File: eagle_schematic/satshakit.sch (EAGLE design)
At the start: 16 parts

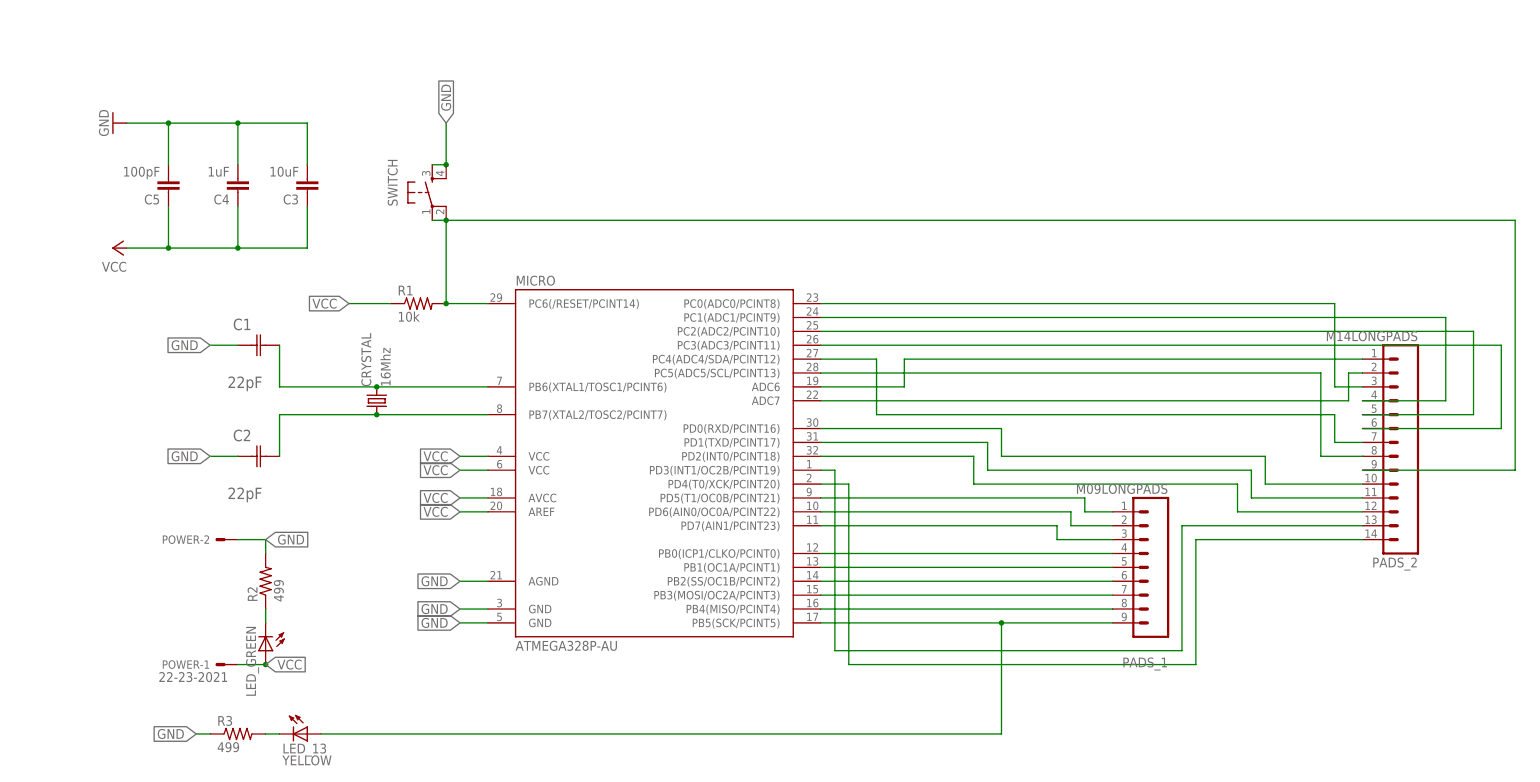
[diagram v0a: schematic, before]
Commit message: v0.2 programming from FTDI cable
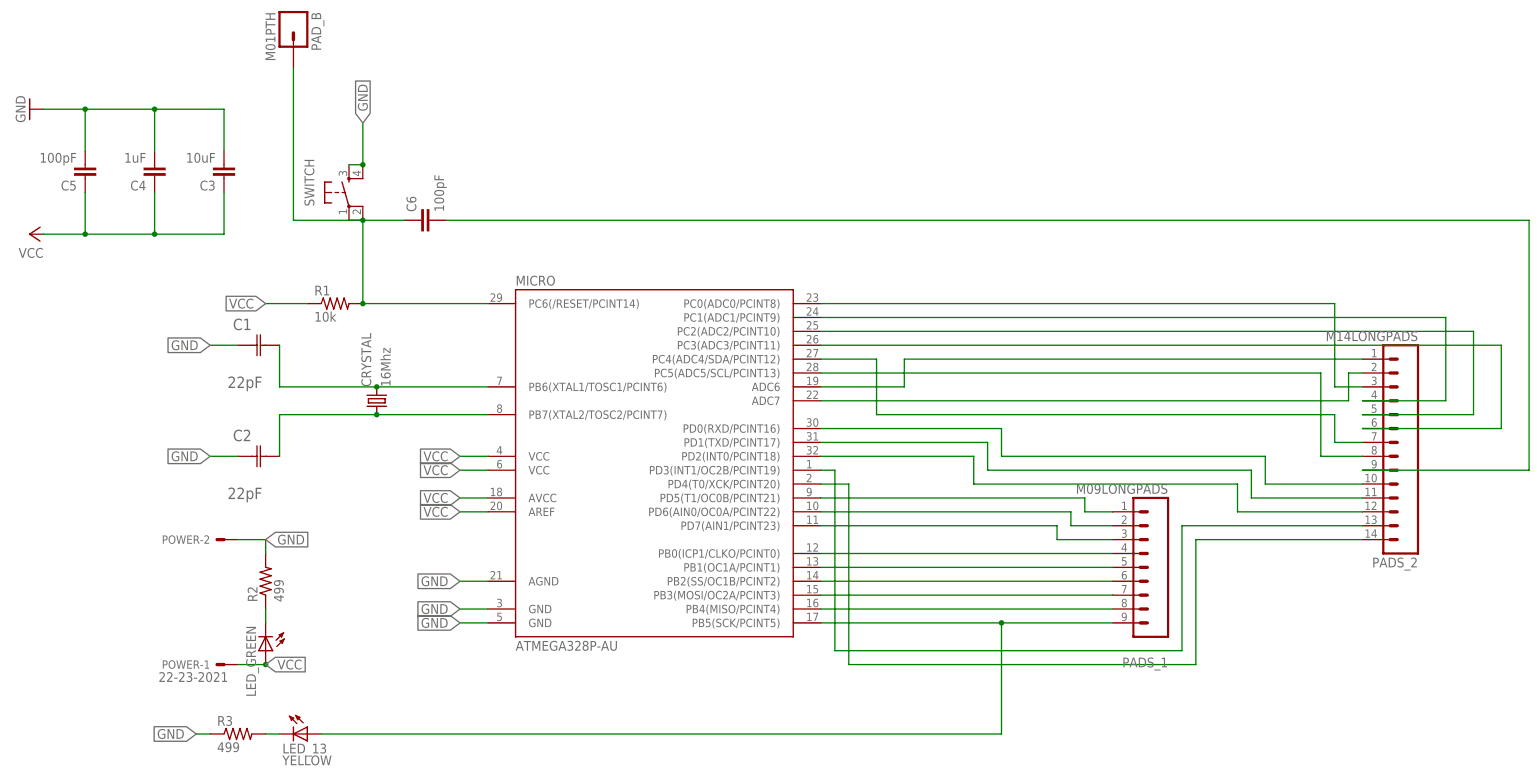
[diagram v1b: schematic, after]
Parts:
- added C6: 100pF, 01_SparkFun:CAP1206
- added PAD_B: M01PTH, 01_SparkFun:M01PTH
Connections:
- new net N$28: C6.1, MICRO.PC6(/RESET/PCINT14), PAD_B.1, R1.2, SWITCH.P, SWITCH.P1
- net N$3: now also C6.2; no longer MICRO.PC6(/RESET/PCINT14), R1.2, SWITCH.P, SWITCH.P1
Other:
- moved on the sheet: C3, C4, C5, R1, SWITCH
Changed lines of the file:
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@@
 <part name="C4" library="01_SparkFun" deviceset="CAP" device="1206" value="1uF"/>
 <part name="C5" library="01_SparkFun" deviceset="CAP" device="1206" value="100pF"/>
+<part name="C6" library="01_SparkFun" deviceset="CAP" device="1206" value="100pF"/>
+<part name="PAD_B" library="01_SparkFun" deviceset="M01" device="PTH"/>
 </parts>
 <sheets>
@@
 <instances>
 <instance part="MICRO" gate="1" x="40.64" y="50.8"/>
-<instance part="P+7" gate="VCC" x="-58.42" y="88.9" rot="R90"/>
+<instance part="P+7" gate="VCC" x="-73.66" y="91.44" rot="R90"/>
 <instance part="CRYSTAL" gate="P" x="-10.16" y="60.96" rot="R90"/>
 <instance part="C1" gate="A" x="-35.56" y="71.12"/>
 <instance part="C2" gate="A" x="-35.56" y="50.8"/>
-<instance part="GND1" gate="1" x="-58.42" y="111.76" rot="R270"/>
-<instance part="R1" gate="G$1" x="-2.54" y="78.74"/>
-<instance part="SWITCH" gate="2" x="0" y="99.06"/>
+<instance part="GND1" gate="1" x="-73.66" y="114.3" rot="R270"/>
+<instance part="R1" gate="G$1" x="-17.78" y="78.74"/>
+<instance part="SWITCH" gate="2" x="-15.24" y="99.06"/>
 <instance part="POWER" gate="-1" x="-38.1" y="12.7" rot="R180"/>
 <instance part="POWER" gate="-2" x="-38.1" y="35.56" rot="R180"/>
@@
 <instance part="R2" gate="G$1" x="-30.48" y="27.94" rot="R90"/>
 <instance part="R3" gate="G$1" x="-35.56" y="0"/>
-<instance part="C3" gate="G$1" x="-22.86" y="101.6" rot="R180"/>
-<instance part="C4" gate="G$1" x="-35.56" y="101.6" rot="R180"/>
-<instance part="C5" gate="G$1" x="-48.26" y="101.6" rot="R180"/>
+<instance part="C3" gate="G$1" x="-38.1" y="104.14" rot="R180"/>
+<instance part="C4" gate="G$1" x="-50.8" y="104.14" rot="R180"/>
+<instance part="C5" gate="G$1" x="-63.5" y="104.14" rot="R180"/>
+<instance part="C6" gate="G$1" x="0" y="93.98" rot="R90"/>
+<instance part="PAD_B" gate="G$1" x="-25.4" y="129.54" rot="R270"/>
 </instances>
 <busses>
@@
 <segment>
 <pinref part="R1" gate="G$1" pin="1"/>
-<wire x1="-7.62" y1="78.74" x2="-15.24" y2="78.74" width="0.1524" layer="91"/>
-<label x="-15.24" y="78.74" size="1.778" layer="95" rot="R180" xref="yes"/>
+<wire x1="-22.86" y1="78.74" x2="-30.48" y2="78.74" width="0.1524" layer="91"/>
+<label x="-30.48" y="78.74" size="1.778" layer="95" rot="R180" xref="yes"/>
 </segment>
 <segment>
@@
 <segment>
 <pinref part="P+7" gate="VCC" pin="VCC"/>
-<wire x1="-55.88" y1="88.9" x2="-48.26" y2="88.9" width="0.1524" layer="91"/>
-<wire x1="-48.26" y1="88.9" x2="-35.56" y2="88.9" width="0.1524" layer="91"/>
+<wire x1="-71.12" y1="91.44" x2="-63.5" y2="91.44" width="0.1524" layer="91"/>
+<wire x1="-63.5" y1="91.44" x2="-50.8" y2="91.44" width="0.1524" layer="91"/>
 <pinref part="C4" gate="G$1" pin="1"/>
-<wire x1="-22.86" y1="88.9" x2="-35.56" y2="88.9" width="0.1524" layer="91"/>
-<wire x1="-35.56" y1="96.52" x2="-35.56" y2="88.9" width="0.1524" layer="91"/>
-<junction x="-35.56" y="88.9"/>
+<wire x1="-38.1" y1="91.44" x2="-50.8" y2="91.44" width="0.1524" layer="91"/>
+<wire x1="-50.8" y1="99.06" x2="-50.8" y2="91.44" width="0.1524" layer="91"/>
+<junction x="-50.8" y="91.44"/>
 <pinref part="C5" gate="G$1" pin="1"/>
-<wire x1="-48.26" y1="96.52" x2="-48.26" y2="88.9" width="0.1524" layer="91"/>
-<junction x="-48.26" y="88.9"/>
+<wire x1="-63.5" y1="99.06" x2="-63.5" y2="91.44" width="0.1524" layer="91"/>
+<junction x="-63.5" y="91.44"/>
 <pinref part="C3" gate="G$1" pin="1"/>
-<wire x1="-22.86" y1="96.52" x2="-22.86" y2="88.9" width="0.1524" layer="91"/>
+<wire x1="-38.1" y1="99.06" x2="-38.1" y2="91.44" width="0.1524" layer="91"/>
 </segment>
 </net>
@@
 <segment>
 <pinref part="GND1" gate="1" pin="GND"/>
-<wire x1="-55.88" y1="111.76" x2="-48.26" y2="111.76" width="0.1524" layer="91"/>
-<wire x1="-48.26" y1="111.76" x2="-35.56" y2="111.76" width="0.1524" layer="91"/>
-<wire x1="-35.56" y1="111.76" x2="-22.86" y2="111.76" width="0.1524" layer="91"/>
-<wire x1="-48.26" y1="104.14" x2="-48.26" y2="111.76" width="0.1524" layer="91"/>
-<junction x="-48.26" y="111.76"/>
-<wire x1="-35.56" y1="104.14" x2="-35.56" y2="111.76" width="0.1524" layer="91"/>
-<junction x="-35.56" y="111.76"/>
+<wire x1="-71.12" y1="114.3" x2="-63.5" y2="114.3" width="0.1524" layer="91"/>
+<wire x1="-63.5" y1="114.3" x2="-50.8" y2="114.3" width="0.1524" layer="91"/>
+<wire x1="-50.8" y1="114.3" x2="-38.1" y2="114.3" width="0.1524" layer="91"/>
+<wire x1="-63.5" y1="106.68" x2="-63.5" y2="114.3" width="0.1524" layer="91"/>
+<junction x="-63.5" y="114.3"/>
+<wire x1="-50.8" y1="106.68" x2="-50.8" y2="114.3" width="0.1524" layer="91"/>
+<junction x="-50.8" y="114.3"/>
 <pinref part="C4" gate="G$1" pin="2"/>
 <pinref part="C5" gate="G$1" pin="2"/>
 <pinref part="C3" gate="G$1" pin="2"/>
-<wire x1="-22.86" y1="104.14" x2="-22.86" y2="111.76" width="0.1524" layer="91"/>
+<wire x1="-38.1" y1="106.68" x2="-38.1" y2="114.3" width="0.1524" layer="91"/>
 </segment>
 <segment>
@@
 <pinref part="SWITCH" gate="2" pin="S"/>
 <pinref part="SWITCH" gate="2" pin="S1"/>
-<wire x1="0" y1="104.14" x2="2.54" y2="104.14" width="0.1524" layer="91"/>
-<wire x1="2.54" y1="104.14" x2="2.54" y2="111.76" width="0.1524" layer="91"/>
-<junction x="2.54" y="104.14"/>
-<label x="2.54" y="111.76" size="1.778" layer="95" rot="R90" xref="yes"/>
+<wire x1="-15.24" y1="104.14" x2="-12.7" y2="104.14" width="0.1524" layer="91"/>
+<wire x1="-12.7" y1="104.14" x2="-12.7" y2="111.76" width="0.1524" layer="91"/>
+<junction x="-12.7" y="104.14"/>
+<label x="-12.7" y="111.76" size="1.778" layer="95" rot="R90" xref="yes"/>
 </segment>
 <segment>
@@
 <wire x1="-40.64" y1="0" x2="-43.18" y2="0" width="0.1524" layer="91"/>
 <label x="-43.18" y="0" size="1.778" layer="95" rot="R180" xref="yes"/>
-</segment>
-</net>
-<net name="N$3" class="0">
-<segment>
-<pinref part="MICRO" gate="1" pin="PC6(/RESET/PCINT14)"/>
-<wire x1="10.16" y1="78.74" x2="2.54" y2="78.74" width="0.1524" layer="91"/>
-<pinref part="R1" gate="G$1" pin="2"/>
-<wire x1="2.54" y1="78.74" x2="2.54" y2="93.98" width="0.1524" layer="91"/>
-<junction x="2.54" y="78.74"/>
-<pinref part="SWITCH" gate="2" pin="P1"/>
-<pinref part="SWITCH" gate="2" pin="P"/>
-<wire x1="2.54" y1="93.98" x2="0" y2="93.98" width="0.1524" layer="91"/>
-<junction x="2.54" y="93.98"/>
-<wire x1="2.54" y1="93.98" x2="198.12" y2="93.98" width="0.1524" layer="91"/>
-<wire x1="198.12" y1="93.98" x2="198.12" y2="48.26" width="0.1524" layer="91"/>
-<pinref part="PADS_2" gate="G$1" pin="9"/>
-<wire x1="198.12" y1="48.26" x2="170.18" y2="48.26" width="0.1524" layer="91"/>
 </segment>
 </net>
@@
 </segment>
 </net>
+<net name="N$28" class="0">
+<segment>
+<pinref part="SWITCH" gate="2" pin="P"/>
+<pinref part="SWITCH" gate="2" pin="P1"/>
+<wire x1="-12.7" y1="93.98" x2="-15.24" y2="93.98" width="0.1524" layer="91"/>
+<junction x="-12.7" y="93.98"/>
+<pinref part="R1" gate="G$1" pin="2"/>
+<wire x1="-12.7" y1="78.74" x2="-12.7" y2="93.98" width="0.1524" layer="91"/>
+<wire x1="-12.7" y1="93.98" x2="-5.08" y2="93.98" width="0.1524" layer="91"/>
+<junction x="-12.7" y="78.74"/>
+<pinref part="MICRO" gate="1" pin="PC6(/RESET/PCINT14)"/>
+<wire x1="10.16" y1="78.74" x2="-12.7" y2="78.74" width="0.1524" layer="91"/>
+<pinref part="C6" gate="G$1" pin="1"/>
+<wire x1="-12.7" y1="93.98" x2="-25.4" y2="93.98" width="0.1524" layer="91"/>
+<wire x1="-25.4" y1="93.98" x2="-25.4" y2="121.92" width="0.1524" layer="91"/>
+<pinref part="PAD_B" gate="G$1" pin="1"/>
+</segment>
+</net>
+<net name="N$3" class="0">
+<segment>
+<pinref part="PADS_2" gate="G$1" pin="9"/>
+<wire x1="200.66" y1="93.98" x2="200.66" y2="48.26" width="0.1524" layer="91"/>
+<wire x1="200.66" y1="48.26" x2="170.18" y2="48.26" width="0.1524" layer="91"/>
+<pinref part="C6" gate="G$1" pin="2"/>
+<wire x1="2.54" y1="93.98" x2="200.66" y2="93.98" width="0.1524" layer="91"/>
+</segment>
+</net>

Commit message: minor fixes
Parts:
- C6: value 100pF -> 100nF
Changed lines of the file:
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@@
 <part name="C4" library="01_SparkFun" deviceset="CAP" device="1206" value="1uF"/>
 <part name="C5" library="01_SparkFun" deviceset="CAP" device="1206" value="100pF"/>
-<part name="C6" library="01_SparkFun" deviceset="CAP" device="1206" value="100pF"/>
+<part name="C6" library="01_SparkFun" deviceset="CAP" device="1206" value="100nF"/>
 <part name="PAD_B" library="01_SparkFun" deviceset="M01" device="PTH"/>
 </parts>

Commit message: minor fixes
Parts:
- C5: value 100pF -> 100nF
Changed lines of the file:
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@@
 <part name="C3" library="01_SparkFun" deviceset="CAP" device="1206" value="10uF"/>
 <part name="C4" library="01_SparkFun" deviceset="CAP" device="1206" value="1uF"/>
-<part name="C5" library="01_SparkFun" deviceset="CAP" device="1206" value="100pF"/>
+<part name="C5" library="01_SparkFun" deviceset="CAP" device="1206" value="100nF"/>
 <part name="C6" library="01_SparkFun" deviceset="CAP" device="1206" value="100nF"/>
 <part name="PAD_B" library="01_SparkFun" deviceset="M01" device="PTH"/>
